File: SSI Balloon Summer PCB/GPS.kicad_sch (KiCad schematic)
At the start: 6 parts, among them J7 GPS antenna, U8 MAX-M10S-00B

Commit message: Fixed ERC - no ERC errors
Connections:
- no-connect marks 8 -> 9
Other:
- note added: "IMPORTANT: for VCC_REF we leave it as not connected because it is PASSIVE - so its unbiased because we plan on the antenna being close to the module. IF THIS CHANGES AND THE ANTENNA IS FAE FROM THE MODULE WE MUST MAKE IT ACTIVE AND CONNECT SHIT ON VCC_REF"
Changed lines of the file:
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@@
 	(generator_version "10.0")
 	(paper "A4")
+	(text "IMPORTANT: for VCC_REF we leave it as\nnot connected because it is PASSIVE - so its\nunbiased because we plan on the antenna being\nclose to the module. IF THIS CHANGES AND THE\nANTENNA IS FAE FROM THE MODULE WE MUST MAKE IT ACTIVE\nAND CONNECT SHIT ON VCC_REF\n"
+		(exclude_from_sim no)
+		(at 241.046 72.136 0)
+		(effects
+			(font
+				(size 1.27 1.27)
+			)
+		)
+	)
 	(text "Output:"
 		(exclude_from_sim no)
@@
 	)
 	(no_connect
+		(at 168.91 77.47)
+	)
+	(no_connect

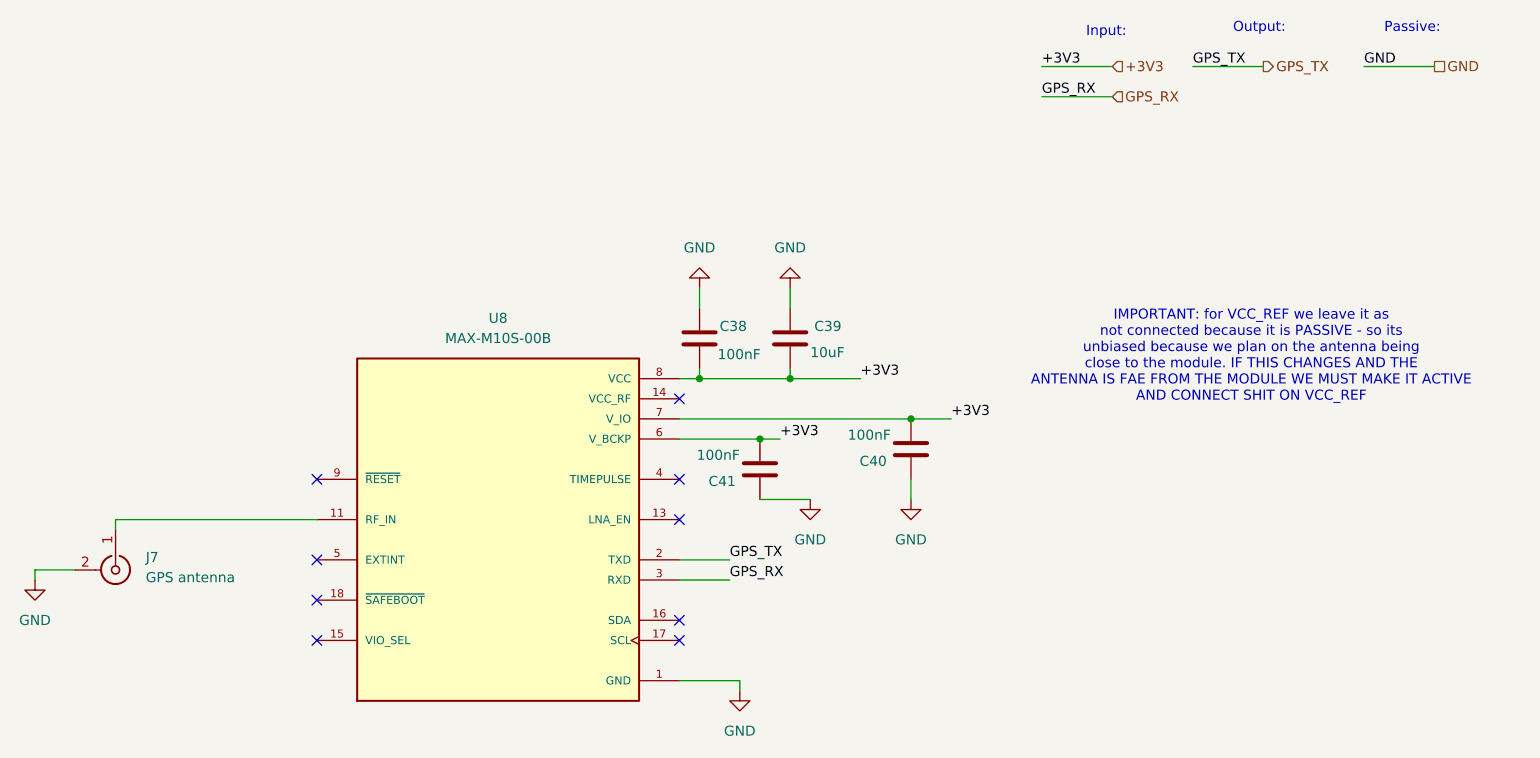
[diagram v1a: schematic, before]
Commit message: Overhauled power symbols for consistency and ERC
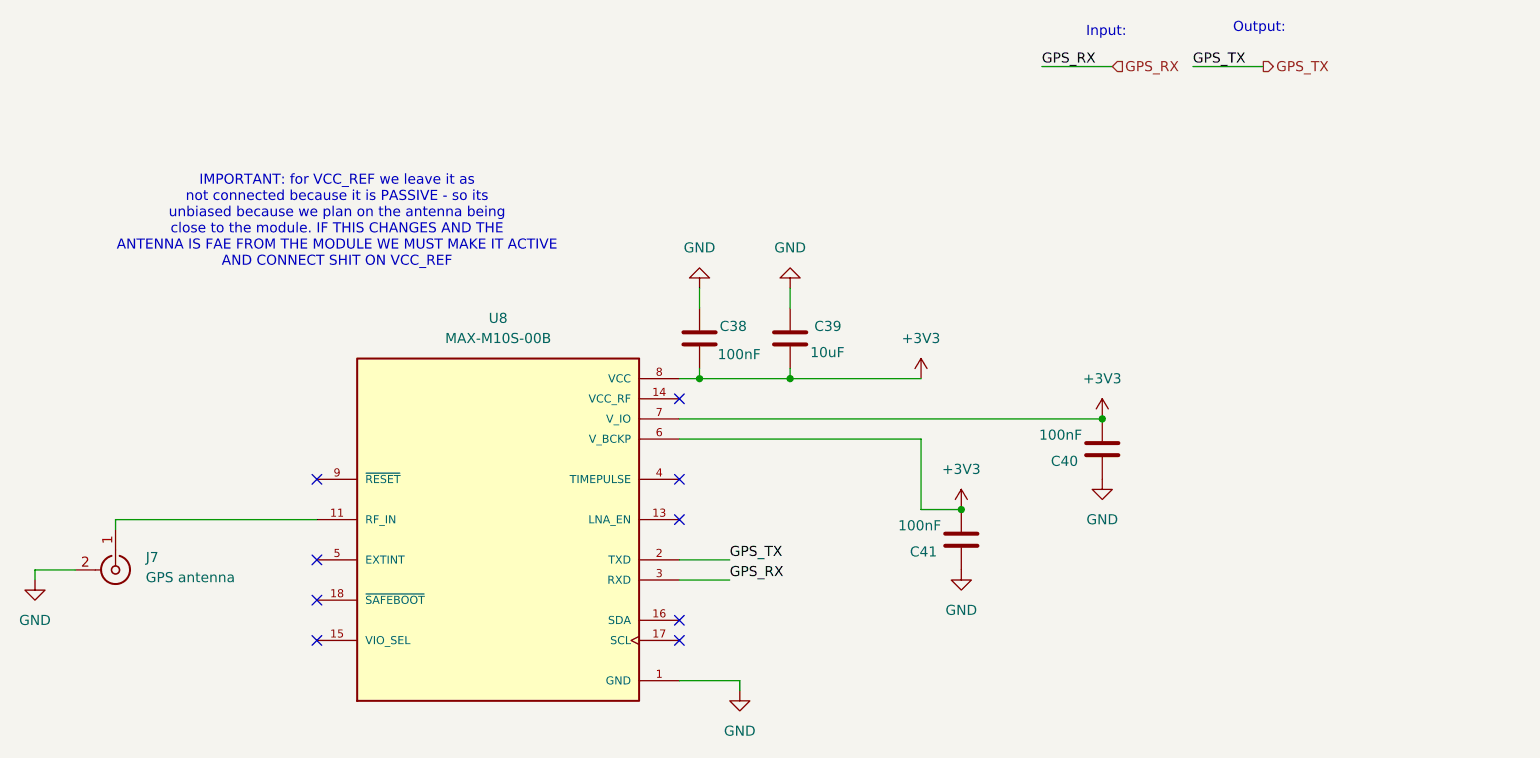
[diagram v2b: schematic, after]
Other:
- note removed: "Passive:"
- moved on the sheet: C40, C41

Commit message: fixed footprints
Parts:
- C38, C40, C41: footprint (none) -> Capacitor_SMD:C_0603_1608Metric
- C39: footprint (none) -> Capacitor_SMD:C_0805_2012Metric
- J7: footprint (none) -> Connector_Coaxial:U.FL_Hirose_U.FL-R-SMT-1_Vertical
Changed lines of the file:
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@@
 			)
 		)
-		(property "Footprint" ""
+		(property "Footprint" "Capacitor_SMD:C_0805_2012Metric"
 			(at 183.8452 73.66 0)
 			(hide yes)
@@
 			)
 		)
-		(property "Footprint" ""
+		(property "Footprint" "Capacitor_SMD:C_0603_1608Metric"
 			(at 172.4152 73.66 0)
 			(hide yes)
@@
 			)
 		)
-		(property "Footprint" ""
+		(property "Footprint" "Connector_Coaxial:U.FL_Hirose_U.FL-R-SMT-1_Vertical"
 			(at 97.79 99.06 0)
 			(hide yes)
@@
 			)
 		)
-		(property "Footprint" ""
+		(property "Footprint" "Capacitor_SMD:C_0603_1608Metric"
 			(at 203.5048 91.44 0)
 			(hide yes)
@@
 			)
 		)
-		(property "Footprint" ""
+		(property "Footprint" "Capacitor_SMD:C_0603_1608Metric"
 			(at 221.2848 80.01 0)
 			(hide yes)
